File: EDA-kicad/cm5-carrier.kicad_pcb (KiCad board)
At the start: 6 copper layers, 82 x 154.8 mm, 121 parts, among them J1 USBC-4-0-CX90MW9-24P1, J2 SIM-G85D1160022HHR, J3 FINGER, J4 SJ2-35894B-SMT-TR, SW1 EG25-switch-CSS-1210MC, SW2 MIC-switch-CSS-1210MC, SW3 CAM-switch-CSS-1210MC, SW4 PROG, SW5 VOL-, SW6 VOL+, SW7 POW, U10 Flash-LED-Lumiled, U2 EG25GGC-128-SGNS, U3 CODEC-TLV320AIC3204IRHBR, U4 BQ25792RQMR, U5 TPS650250RHBR, U6 BAT-CONNECTOR-FLTS22WR00, U7 22V-boost-AP3032KTR-G1, U8 MP3429GL-Z, U9 FPC15pin-1mm-pitch-F52Q-1A7H1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

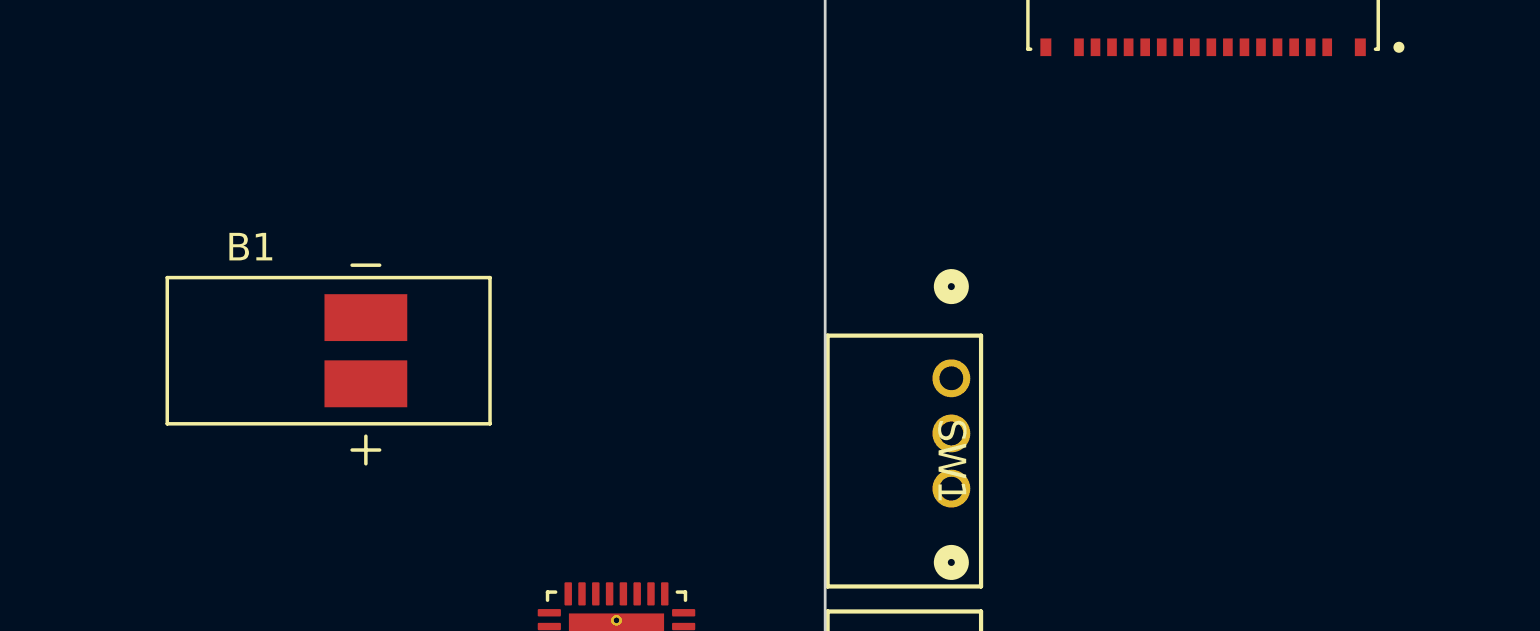
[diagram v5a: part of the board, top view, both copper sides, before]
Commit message: set everything except from power to DNP
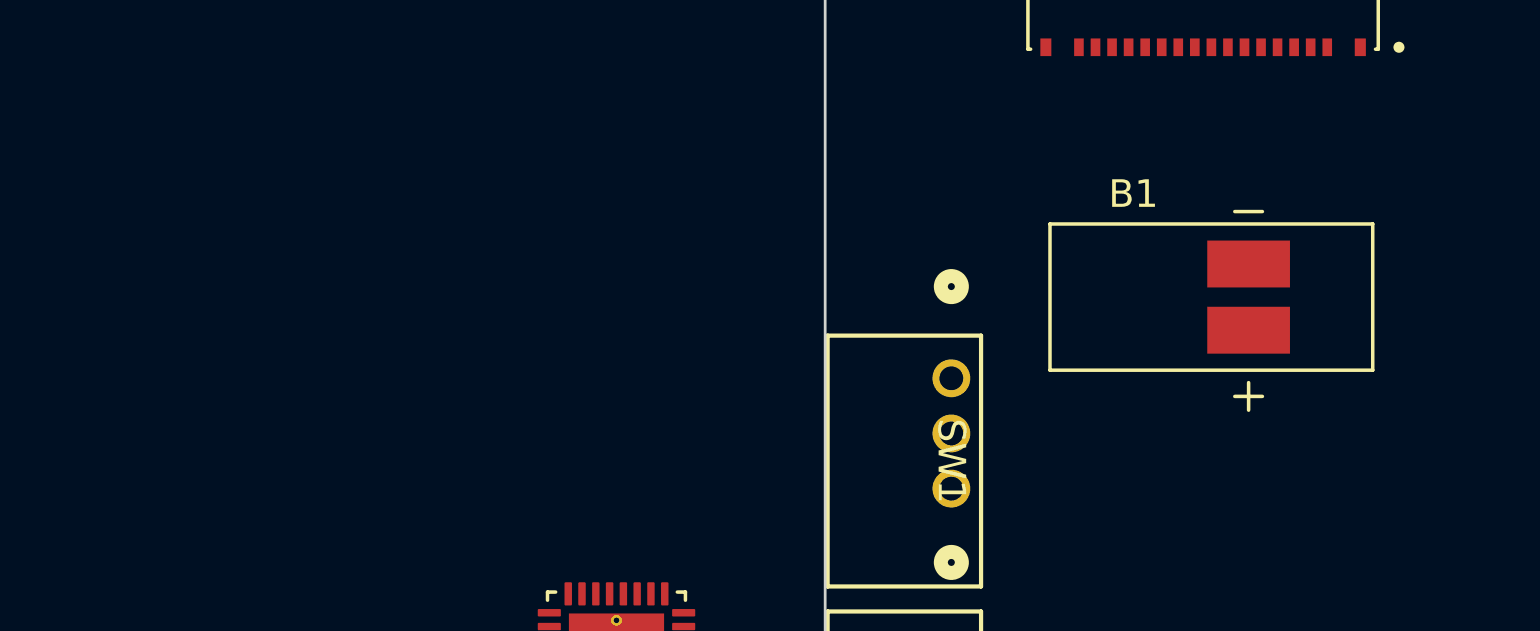
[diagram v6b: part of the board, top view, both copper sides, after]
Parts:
- moved B1 32.1 mm to (68.0, 146.1)
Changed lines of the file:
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@@
 		(sheetname "/Audio/")
 		(sheetfile "audio.kicad_sc.kicad_sch")
-		(attr smd)
+		(attr smd dnp)
 		(fp_line
 			(start -2.75 -3.2)
@@
 		(sheetname "/")
 		(sheetfile "cm5-carrier.kicad_sch")
-		(attr smd)
+		(attr smd dnp)
 		(fp_line
 			(start -0.718 -0.448)
@@
 		(sheetname "/")
 		(sheetfile "cm5-carrier.kicad_sch")
-		(attr smd)
+		(attr smd dnp)
 		(fp_line
 			(start -0.718 -0.448)
@@
 		(sheetname "/USB C/")
 		(sheetfile "USB-C.kicad_sch")
-		(attr smd)
+		(attr smd dnp)
 		(fp_line
 			(start -0.5715 -0.4191)
@@
 		(sheetname "/Camera/")
 		(sheetfile "camera.kicad_sch")
-		(attr smd)
+		(attr smd dnp)
 		(fp_text user "${REFERENCE}"
 			(at 0.127 -0.508 270)
@@
 		(sheetname "/GSM-GPS/")
 		(sheetfile "GSM-GPS.kicad_sch")
-		(attr smd)
+		(attr smd dnp)
 		(fp_poly
 			(pts
@@
 		(sheetname "/Camera/")
 		(sheetfile "camera.kicad_sch")
-		(attr smd)
+		(attr smd dnp)
 		(fp_text user "${REFERENCE}"
 			(at 0.127 -0.508 270)
@@
 		(sheetname "/USB C/")
 		(sheetfile "USB-C.kicad_sch")
-		(attr smd)
+		(attr smd dnp)
 		(fp_poly
 			(pts
@@
 		(sheetname "/Buttons/")
 		(sheetfile "buttons.kicad_sch")
-		(attr smd)
+		(attr smd dnp)
 		(fp_line
 			(start -4.0259 1.8796)
@@
 		(sheetname "/Audio/")
 		(sheetfile "audio.kicad_sc.kicad_sch")
-		(attr smd)
+		(attr smd dnp)
 		(fp_line
 			(start -7.5 -0.47)
@@
 		(sheetname "/Audio/")
 		(sheetfile "audio.kicad_sc.kicad_sch")
-		(attr smd)
+		(attr smd dnp)
 		(fp_line
 			(start 7.5 3)
@@
 		(sheetname "/Vibration/")
 		(sheetfile "vibration.kicad_sch")
-		(attr smd)
+		(attr smd dnp)
 		(fp_line
 			(start -2.21 -0.9)
@@
 		(sheetname "/Buttons/")
 		(sheetfile "buttons.kicad_sch")
-		(attr smd)
+		(attr smd dnp)
 		(fp_line
 			(start -4.0259 1.8796)
@@
 		(sheetname "/")
 		(sheetfile "cm5-carrier.kicad_sch")
-		(attr smd)
+		(attr smd dnp)
 		(fp_line
 			(start -0.718 -0.448)
@@
 		(sheetname "/Audio/")
 		(sheetfile "audio.kicad_sc.kicad_sch")
-		(attr smd)
+		(attr smd dnp)
 		(fp_circle
 			(center 0 0)
@@
 		(sheetname "/Screen/")
 		(sheetfile "screen.kicad_sch")
-		(attr smd)
+		(attr smd dnp)
 		(fp_text user "${REFERENCE}"
 			(at 0.127 -0.508 0)
@@
 		(sheetname "/Audio/")
 		(sheetfile "audio.kicad_sc.kicad_sch")
-		(attr smd)
+		(attr smd dnp)
 		(fp_line
 			(start -0.28 -0.625)
@@
 		(sheetname "/Buttons/")
 		(sheetfile "buttons.kicad_sch")
-		(attr smd)
+		(attr smd dnp)
 		(fp_line
 			(start 4.0259 -1.8796)
@@
 		(sheetname "/Buttons/")
 		(sheetfile "buttons.kicad_sch")
-		(attr smd)
+		(attr smd dnp)
 		(fp_line
 			(start -4.0259 1.8796)
@@
 		(sheetname "/Audio/")
 		(sheetfile "audio.kicad_sc.kicad_sch")
-		(attr smd)
+		(attr smd dnp)
 		(fp_line
 			(start 2.5 -2.5)
@@
 		(sheetname "/Flashlight/")
 		(sheetfile "flashlight.kicad_sch")
-		(attr smd)
+		(attr smd dnp)
 		(fp_line
 			(start -1 -1.59)
@@
 		(sheetname "/Screen/")
 		(sheetfile "screen.kicad_sch")
-		(attr smd)
+		(attr smd dnp)
 		(fp_text user "${REFERENCE}"
 			(at 0.127 -0.508 0)
@@
 	(footprint "SPIRIT-footprints:VIBRATION-PUI_HD-EMB1205-3-SC-R"
 		(layer "F.Cu")
-		(at 36 148)
+		(at 68 146.056399)
 		(property "Reference" "B1"
 			(at -2.825 -3.735 0)
@@
 		(sheetname "/Vibration/")
 		(sheetfile "vibration.kicad_sch")
-		(attr smd)
+		(attr smd dnp)
 		(fp_line
 			(start -5.85 -2.65)
@@
 		(sheetname "/Fingerprint/")
 		(sheetfile "fingerprint.kicad_sch")
-		(attr smd)
+		(attr smd dnp)
 		(fp_line
 			(start -3.6322 -2.0447)
@@
 		(sheetname "/Vibration/")
 		(sheetfile "vibration.kicad_sch")
-		(attr smd)
+		(attr smd dnp)
 		(fp_line
 			(start -0.28 -0.625)
@@
 		(sheetname "/")
 		(sheetfile "cm5-carrier.kicad_sch")
-		(attr smd)
+		(attr smd dnp)
 		(fp_line
 			(start -0.7747 -0.4191)
@@
 		(sheetname "/")
 		(sheetfile "cm5-carrier.kicad_sch")
-		(attr smd)
+		(attr smd dnp)
 		(fp_line
 			(start -0.718 -0.448)
@@
 		(sheetname "/Fingerprint/")
 		(sheetfile "fingerprint.kicad_sch")
-		(attr smd)
+		(attr smd dnp)
 		(fp_line
 			(start -0.28 0.625)
@@
 		(sheetname "/Audio/")
 		(sheetfile "audio.kicad_sc.kicad_sch")
-		(attr smd)
+		(attr smd dnp)
 		(fp_line
 			(start -0.2 -0.1)
@@
 		(sheetname "/Vibration/")
 		(sheetfile "vibration.kicad_sch")
-		(attr smd)
+		(attr smd dnp)
 		(fp_line
 			(start -0.68 -1.214)
@@
 		(sheetname "/Screen/")
 		(sheetfile "screen.kicad_sch")
-		(attr smd)
+		(attr smd dnp)
 		(fp_line
 			(start -6.35 -1.75)
@@
 		(sheetname "/Audio/")
 		(sheetfile "audio.kicad_sc.kicad_sch")
-		(attr smd)
+		(attr smd dnp)
 		(fp_line
 			(start -0.2 -0.1)
@@
 		(sheetname "/USB C/")
 		(sheetfile "USB-C.kicad_sch")
-		(attr smd)
+		(attr smd dnp)
 		(fp_poly
 			(pts
@@
 		(sheetname "/GSM-GPS/")
 		(sheetfile "GSM-GPS.kicad_sch")
-		(attr smd)
+		(attr smd dnp)
 		(fp_line
 			(start -4.88 7)
@@
 		(sheetname "/Flashlight/")
 		(sheetfile "flashlight.kicad_sch")
-		(attr smd)
+		(attr smd dnp)
 		(fp_line
 			(start -0.68 -1.214)
@@
 		(sheetname "/")
 		(sheetfile "cm5-carrier.kicad_sch")
-		(attr smd)
+		(attr smd dnp)
 		(fp_line
 			(start 33 51.5)
@@
 		(sheetname "/Camera/")
 		(sheetfile "camera.kicad_sch")
-		(attr smd)
+		(attr smd dnp)
 		(fp_poly
 			(pts

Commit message: setup layers
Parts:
- added ?: , , F.Cu at (79.1, 140.6)
- R25: value 1K-05W-0805-RES_ERJP06J102V -> 1K
- U4: footprint SPIRIT-footprints:CHARGER-SWITCHER-RTE0016C -> SPIRIT-footprints:charger-bq25792-QFN40P400X400X100-29N
- moved R7 128.0 mm to (71.1, 159.5)
- moved R4 109.7 mm to (66.5, 159.5)
- moved U4 109.3 mm to (69.2, 154.3)
- moved C17 108.3 mm to (70.8, 151.1)
- moved C22 107.9 mm to (70.8, 144.1)
- moved C19 105.3 mm to (70.8, 148.3)
- moved C20 103.6 mm to (70.8, 146.9)
- moved C21 101.9 mm to (70.8, 145.5)
- moved C9 101.1 mm to (74.2, 152.5), turned to 180 degrees
- moved C18 93.9 mm to (70.8, 149.7)
- moved B1 37.4 mm to (30.8, 142.0)
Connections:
- C10 pad 2: GND -> BACKLIGHT-
- C11 pad 2: GND -> BACKLIGHT-
- C12 pad 2: GND -> BACKLIGHT-
- C13 pad 2: GND -> BACKLIGHT-
- C14 pad 2: GND -> BACKLIGHT-
- C17 pad 2: GND -> BACKLIGHT-
- C18 pad 2: GND -> BACKLIGHT-
- C19 pad 2: GND -> BACKLIGHT-
- C20 pad 2: GND -> BACKLIGHT-
- C21 pad 2: GND -> BACKLIGHT-
- C22 pad 2: GND -> BACKLIGHT-
- C23 pad 2: GND -> BACKLIGHT-
- C24 pad 2: GND -> BACKLIGHT-
- C25 pad 2: GND -> BACKLIGHT-
- C26 pad 2: GND -> BACKLIGHT-
- C27 pad 2: GND -> BACKLIGHT-
- C28 pad 2: GND -> BACKLIGHT-
- C29 pad 2: GND -> BACKLIGHT-
- C30 pad 2: GND -> BACKLIGHT-
- C31 pad 2: GND -> BACKLIGHT-
- C33 pad 2: GND -> BACKLIGHT-
- C34 pad 2: GND -> BACKLIGHT-
- C35 pad 2: GND -> BACKLIGHT-
- C36 pad 2: GND -> BACKLIGHT-
- C37 pad 2: GND -> BACKLIGHT-
- C38 pad 2: GND -> BACKLIGHT-
- C39 pad 2: GND -> BACKLIGHT-
- C41 pad 1: GND -> BACKLIGHT-
- C5 pad 1: GND -> BACKLIGHT-
- C6 pad 2: GND -> BACKLIGHT-
- C7 pad 2: GND -> BACKLIGHT-
- C8 pad 2: GND -> BACKLIGHT-
- C9 pad 2: GND -> BACKLIGHT-
- DIS1 pad 1: GND -> BACKLIGHT-
- DIS1 pad 10: GND -> BACKLIGHT-
- DIS1 pad 13: GND -> BACKLIGHT-
- DIS1 pad 16: GND -> BACKLIGHT-
- DIS1 pad 19: GND -> BACKLIGHT-
- DIS1 pad 2: unconnected-(DIS1-Pad2) -> 22V
- DIS1 pad 20: GND -> BACKLIGHT-
- DIS1 pad 25: VCC -> 1V8
- DIS1 pad 30: VCC -> 3V3B
- DIS1 pad 31: GND -> BACKLIGHT-
- DIS1 pad 4: GND -> BACKLIGHT-
- DIS1 pad 7: GND -> BACKLIGHT-
- J1 pad A1: GND -> BACKLIGHT-
- J1 pad A12: GND -> BACKLIGHT-
- J1 pad B1: GND -> BACKLIGHT-
- J1 pad B12: GND -> BACKLIGHT-
- J1 pad SH1: GND -> BACKLIGHT-
- J1 pad SH2: GND -> BACKLIGHT-
- J1 pad SH3: GND -> BACKLIGHT-
- J1 pad SH4: GND -> BACKLIGHT-
- J2 pad C5: GND -> BACKLIGHT-
- J2 pad S1: GND -> BACKLIGHT-
- J2 pad S2: GND -> BACKLIGHT-
- J2 pad S3: GND -> BACKLIGHT-
- J3 pad 1: GND -> BACKLIGHT-
- MK1 pad 2: GND -> BACKLIGHT-
- MK1 pad 3: GND -> BACKLIGHT-
- Module1 pad 1: GND -> BACKLIGHT-
- Module1 pad 107: GND -> BACKLIGHT-
- Module1 pad 108: GND -> BACKLIGHT-
- Module1 pad 113: GND -> BACKLIGHT-
- Module1 pad 114: GND -> BACKLIGHT-
- Module1 pad 119: GND -> BACKLIGHT-
- Module1 pad 120: GND -> BACKLIGHT-
- Module1 pad 125: GND -> BACKLIGHT-
- Module1 pad 126: GND -> BACKLIGHT-
- Module1 pad 13: GND -> BACKLIGHT-
- Module1 pad 131: GND -> BACKLIGHT-
- Module1 pad 132: GND -> BACKLIGHT-
- Module1 pad 137: GND -> BACKLIGHT-
- Module1 pad 138: GND -> BACKLIGHT-
- Module1 pad 14: GND -> BACKLIGHT-
- Module1 pad 144: GND -> BACKLIGHT-
- Module1 pad 150: GND -> BACKLIGHT-
- Module1 pad 155: GND -> BACKLIGHT-
- Module1 pad 156: GND -> BACKLIGHT-
- Module1 pad 161: GND -> BACKLIGHT-
- Module1 pad 162: GND -> BACKLIGHT-
- Module1 pad 167: GND -> BACKLIGHT-
- Module1 pad 168: GND -> BACKLIGHT-
- Module1 pad 173: GND -> BACKLIGHT-
- Module1 pad 174: GND -> BACKLIGHT-
- Module1 pad 179: GND -> BACKLIGHT-
- Module1 pad 180: GND -> BACKLIGHT-
- Module1 pad 185: GND -> BACKLIGHT-
- Module1 pad 186: GND -> BACKLIGHT-
- Module1 pad 191: GND -> BACKLIGHT-
- Module1 pad 192: GND -> BACKLIGHT-
- Module1 pad 197: GND -> BACKLIGHT-
- Module1 pad 198: GND -> BACKLIGHT-
- Module1 pad 2: GND -> BACKLIGHT-
- Module1 pad 22: GND -> BACKLIGHT-
- Module1 pad 23: GND -> BACKLIGHT-
- Module1 pad 32: GND -> BACKLIGHT-
- Module1 pad 33: GND -> BACKLIGHT-
- Module1 pad 42: GND -> BACKLIGHT-
- Module1 pad 43: GND -> BACKLIGHT-
- Module1 pad 52: GND -> BACKLIGHT-
- Module1 pad 53: GND -> BACKLIGHT-
- Module1 pad 60: GND -> BACKLIGHT-
- Module1 pad 66: GND -> BACKLIGHT-
- Module1 pad 71: GND -> BACKLIGHT-
- Module1 pad 74: GND -> BACKLIGHT-
- Module1 pad 8: GND -> BACKLIGHT-
- Module1 pad 98: GND -> BACKLIGHT-
- Q3 pad 3: GND -> BACKLIGHT-
- Q4 pad 3: GND -> BACKLIGHT- (x2)
- R10 pad 1: GND -> BACKLIGHT-
- R12 pad 1: GND -> BACKLIGHT-
- R15 pad 2: GND -> BACKLIGHT-
- R16 pad 2: GND -> BACKLIGHT-
- R20 pad 1: Net-(U7-FB) -> BACKLIGHT-
- R20 pad 2: GND -> BACKLIGHT-
- R3 pad 1: GND -> BACKLIGHT-
- R5 pad 1: GND -> BACKLIGHT-
- R7 pad 2: GND -> BACKLIGHT-
- TVS-PUSB1 pad 2: GND -> BACKLIGHT-
- U3 pad 17: GND -> BACKLIGHT-
- U3 pad 28: GND -> BACKLIGHT-
- U3 pad 7: GND -> BACKLIGHT-
- U4 pad 10: GND -> BACKLIGHT-
- U4 pad 11: GND -> BACKLIGHT-
- U5 pad 2: GND -> BACKLIGHT-
- U5 pad 26: GND -> BACKLIGHT-
- U5 pad 7: GND -> BACKLIGHT-
- U6 pad 4: GND -> BACKLIGHT-
- U7 pad 2: GND -> BACKLIGHT-
- U7 pad 3: Net-(U7-FB) -> BACKLIGHT-
- U8 pad 7: GND -> BACKLIGHT-
- U9 pad 1: GND -> BACKLIGHT-
- U9 pad 10: GND -> BACKLIGHT-
- U9 pad 4: GND -> BACKLIGHT-
- ZD1 pad 2: GND -> BACKLIGHT-
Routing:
- net SYS: track 0.00 -> 8.40 mm
- net (no net): track 0.00 -> 1.62 mm, vias 0 -> 1

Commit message: minor pcb progress
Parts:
- removed ?: , 
- added REF**: Symbol_HighVoltage_Triangle_17x15mm_Copper, Symbol:Symbol_HighVoltage_Triangle_17x15mm_Copper, F.Cu at (39.1, 50.7)
- moved R9 99.3 mm to (80.6, 152.1), turned to 180 degrees
- moved C7 94.1 mm to (80.6, 149.1)
- moved C8 93.5 mm to (80.6, 150.6)
- moved C17 4.52 mm to (75.2, 150.1)
- moved C18 4.52 mm to (75.2, 148.7)
- moved C19 4.52 mm to (75.2, 147.3)
- moved C20 4.52 mm to (75.2, 145.9)
- moved C21 4.52 mm to (75.2, 144.5)
- moved C22 4.52 mm to (75.2, 143.1)
- moved U4 4.52 mm to (73.6, 153.3)
- moved C9 3.04 mm to (77.1, 151.3), turned to 0 degrees
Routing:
- net BAT+: track 0.00 -> 28.0 mm
- net BACKLIGHT-: track 0.00 -> 17.9 mm, vias 0 -> 1
- net SYS: track 8.40 -> 16.5 mm, vias 0 -> 2
- net Net-(U4-BATP): track 0.00 -> 6.64 mm
- net (no net): track 1.62 -> 0.00 mm, vias 1 -> 6
- net Net-(U4-SDRV): track 0.00 -> 1.28 mm
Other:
- board text added: "thermal vias under BQ???"
